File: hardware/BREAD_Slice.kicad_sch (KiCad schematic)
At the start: 15 parts, among them J1 Conn_01x10_Female, J2 I2C_01x04

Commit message: Initial commit
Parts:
- removed C1, C3, C4: 22uF, Capacitor_SMD:C_1206_3216Metric, symbol Device:C_Small
- removed C2: 100nF, Capacitor_SMD:C_1206_3216Metric, symbol Device:C_Small
- removed D1: WS2812B_5050, SparkFun-LED:WS2812-5050-4PIN, symbol SparkFun-LED:WS2812B_5050
- removed HS1: Heatsink_Pad, SparkFun-Fuse:Thermal Pad, symbol Mechanical:Heatsink_Pad
- removed J2: I2C_01x04, Connector_JST:JST_SH_SM04B-SRSS-TB_1x04-1MP_P1.00mm_Horizontal, symbol SparkFun-Connector:I2C_01x04
- removed L1: 4.7uH, Inductor_SMD:L_1210_3225Metric, symbol Device:L_Small
- removed U1: ~, Package_TO_SOT_SMD:TSOT-23-6, symbol SparkFun-DiscreteSemi:AP63205
- added C1, C2: 10uF_t, OCI_UPL_FOOTPRINTS:C_2312, symbol BREAD_Slice-rescue:10uF_t-OCI_UPL_2_Capacitors
- added J2, J3, J4, J5, J6: Screw_Terminal_01x03, TerminalBlock_TE-Connectivity:TerminalBlock_TE_282834-3_1x03_P2.54mm_Horizontal, symbol Connector:Screw_Terminal_01x03
- added J7: Conn_01x03_Male, Connector_PinSocket_2.54mm:PinSocket_1x03_P2.54mm_Vertical, symbol BREAD_Slice-rescue:Conn_01x03_Male-Connector
- added J8: Screw_Terminal_01x02, TerminalBlock_TE-Connectivity:TerminalBlock_TE_282834-2_1x02_P2.54mm_Horizontal, symbol Connector:Screw_Terminal_01x02
- added Logo1: Logo_Open_Hardware_Small, Symbol:OSHW-Symbol_6.7x6mm_SilkScreen, symbol Graphic:Logo_Open_Hardware_Small
- H1, H4: footprint MountingHole:MountingHole_5mm -> MountingHole:MountingHole_3.2mm_M3_DIN965_Pad
- H2: renamed from H3; footprint MountingHole:MountingHole_5mm -> MountingHole:MountingHole_3.2mm_M3_DIN965_Pad
- H3: renamed from H2; footprint MountingHole:MountingHole_5mm -> MountingHole:MountingHole_3.2mm_M3_DIN965_Pad
- J1: symbol Connector:Conn_01x10_Female -> BREAD_Slice-rescue:Conn_01x10_Female-Connector
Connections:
- net +12V: now also A1.30 (VIN), C1.1, J7.3 (Pin_3)
- net +5V: now also C2.1
- net GND: now also C1.2, C2.2, J2.3 (Pin_3), J3.3 (Pin_3), J4.3 (Pin_3), J5.3 (Pin_3), J6.3 (Pin_3), J8.2 (Pin_2)
- net PWM3: now reaches A1.12 (D9)
- net PWM3: now also J6.1 (Pin_1)
- net PWM4: now reaches A1.13 (D10)
- net PWM4: now also J3.1 (Pin_1)
- net PWM5: now reaches A1.14 (D11)
- net PWM5: now also J5.1 (Pin_1)
- net PWM2: now reaches A1.9 (D6)
- net PWM2: now also J4.1 (Pin_1)
- net LED renamed PWM1
- net PWM1: now also J2.1 (Pin_1)
- new net CSTM: J7.2 (Pin_2), J8.1 (Pin_1)
- new net PWR: J2.2 (Pin_2), J3.2 (Pin_2), J4.2 (Pin_2), J5.2 (Pin_2), J7.1 (Pin_1)
- no-connect marks 22 -> 16
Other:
- moved on the sheet: A1, H1, H2, H3, H4, J1

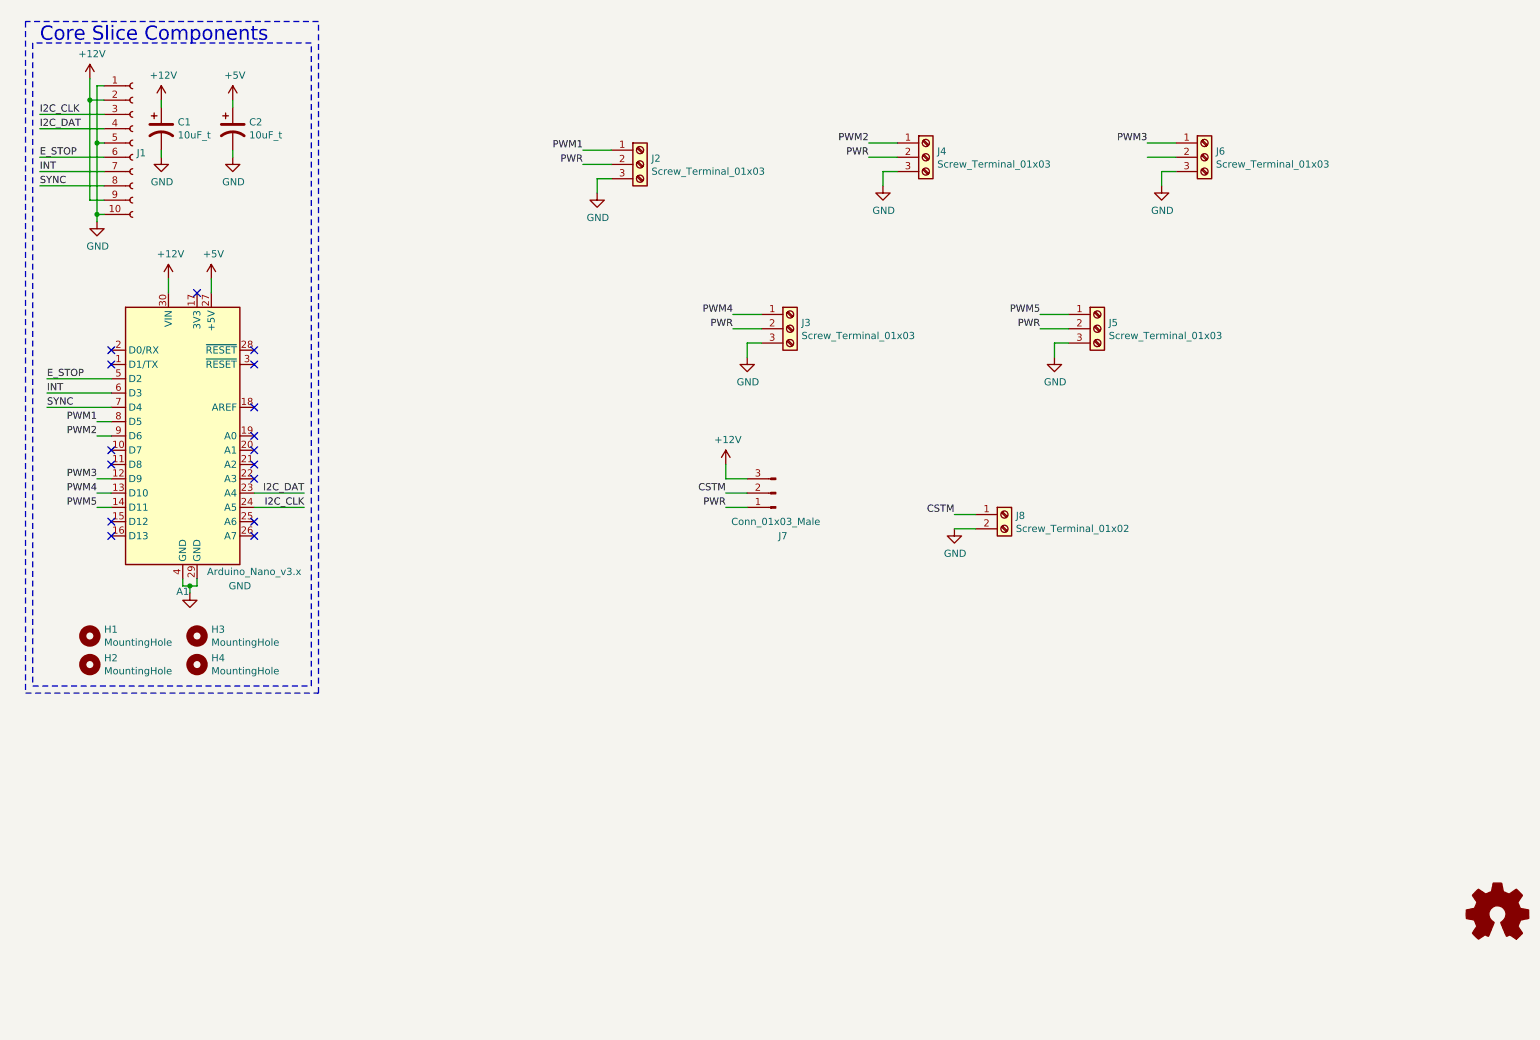
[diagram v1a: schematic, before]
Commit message: changed custom selection method to be correct and offer 5V, new BREAD core
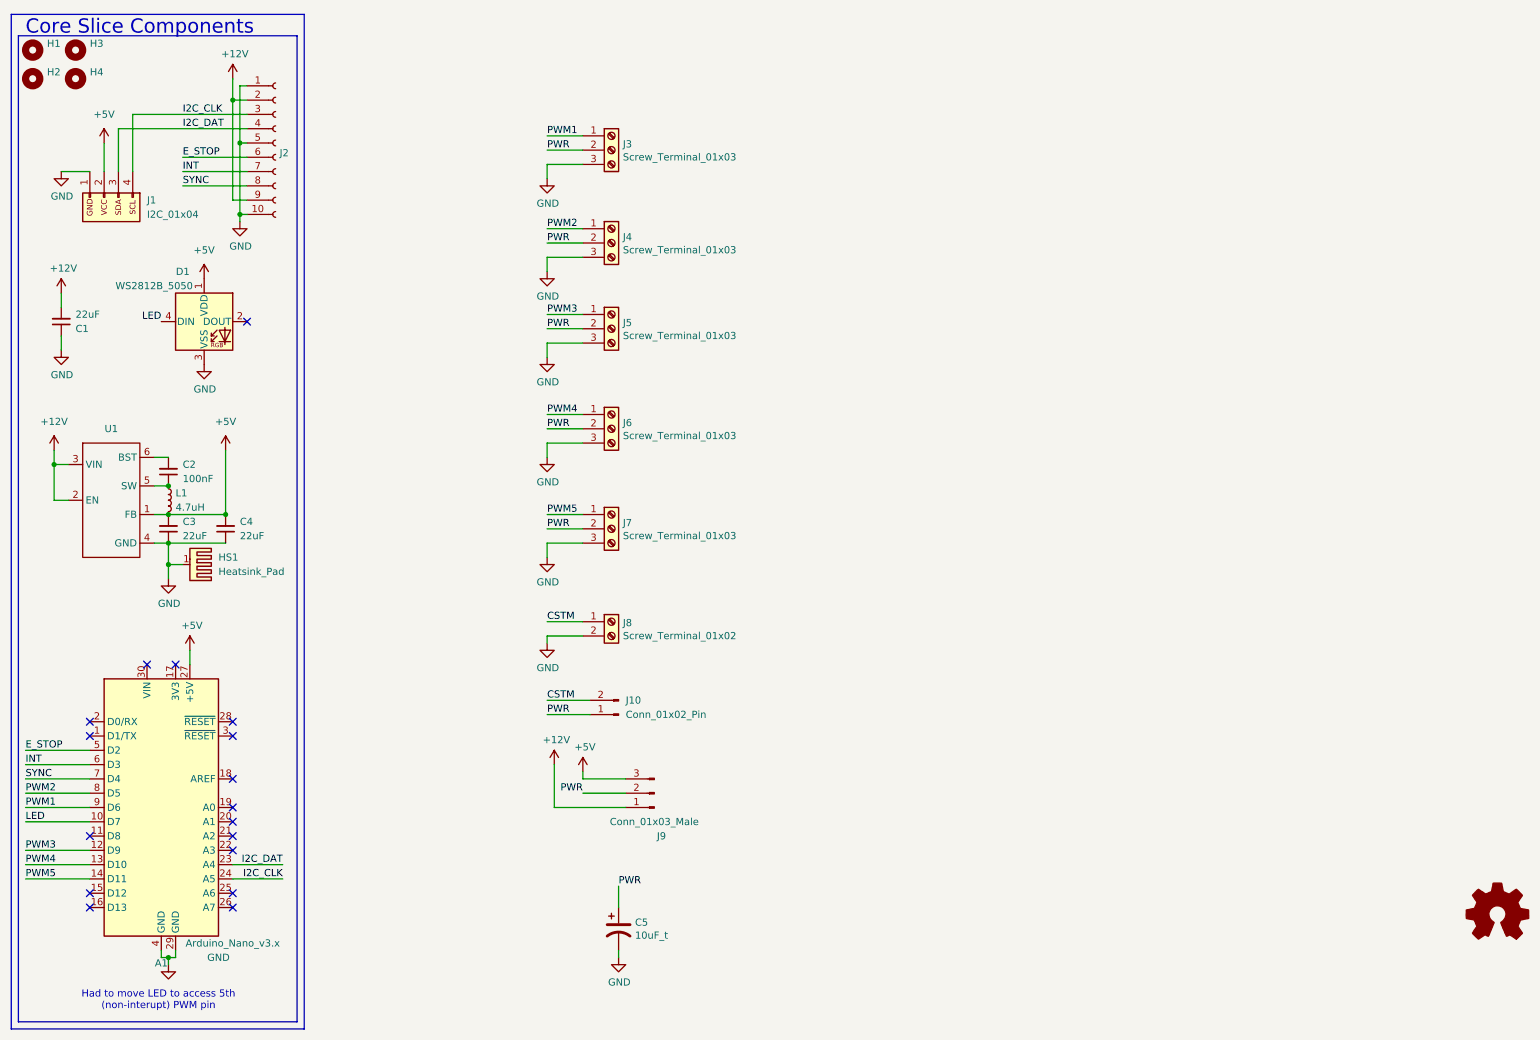
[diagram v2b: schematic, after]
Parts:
- removed C1, C2: 10uF_t, OCI_UPL_FOOTPRINTS:C_2312, symbol BREAD_Slice-rescue:10uF_t-OCI_UPL_2_Capacitors
- removed J2: Screw_Terminal_01x03, TerminalBlock_TE-Connectivity:TerminalBlock_TE_282834-3_1x03_P2.54mm_Horizontal, symbol Connector:Screw_Terminal_01x03
- removed J7: Conn_01x03_Male, Connector_PinSocket_2.54mm:PinSocket_1x03_P2.54mm_Vertical, symbol BREAD_Slice-rescue:Conn_01x03_Male-Connector
- removed Logo1: Logo_Open_Hardware_Small, Symbol:OSHW-Symbol_6.7x6mm_SilkScreen, symbol Graphic:Logo_Open_Hardware_Small
- added C1, C3, C4: 22uF, Capacitor_SMD:C_1206_3216Metric, symbol Device:C_Small
- added C2: 100nF, Capacitor_SMD:C_1206_3216Metric, symbol Device:C_Small
- added C5: 10uF_t, Capacitor_SMD:C_2220_5750Metric_Pad1.97x5.40mm_HandSolder, symbol BREAD_Slice-rescue:10uF_t-OCI_UPL_2_Capacitors
- added D1: WS2812B_5050, SparkFun-LED:WS2812-5050-4PIN, symbol SparkFun-LED:WS2812B_5050
- added HS1: Heatsink_Pad, KML-Custom:Thermal Pad, symbol Mechanical:Heatsink_Pad
- added J1: I2C_01x04, Connector_JST:JST_SH_SM04B-SRSS-TB_1x04-1MP_P1.00mm_Horizontal, symbol SparkFun-Connector:I2C_01x04
- added J10: Conn_01x02_Pin, Connector_PinSocket_2.54mm:PinSocket_1x02_P2.54mm_Vertical, symbol Connector:Conn_01x02_Pin
- added J7: Screw_Terminal_01x03, TerminalBlock_Phoenix:TerminalBlock_Phoenix_MPT-0,5-3-2.54_1x03_P2.54mm_Horizontal, symbol Connector:Screw_Terminal_01x03
- added J9: Conn_01x03_Male, Connector_PinSocket_2.54mm:PinSocket_1x03_P2.54mm_Vertical, symbol BREAD_Slice-rescue:Conn_01x03_Male-Connector
- added L1: 4.7uH, Inductor_SMD:L_1210_3225Metric, symbol Device:L_Small
- added U1: ~, Package_TO_SOT_SMD:TSOT-23-6, symbol SparkFun-DiscreteSemi:AP63205
- H1, H4: footprint MountingHole:MountingHole_3.2mm_M3_DIN965_Pad -> MountingHole:MountingHole_5mm
- H2: renamed from H3; footprint MountingHole:MountingHole_3.2mm_M3_DIN965_Pad -> MountingHole:MountingHole_5mm
- H3: renamed from H2; footprint MountingHole:MountingHole_3.2mm_M3_DIN965_Pad -> MountingHole:MountingHole_5mm
- J2: renamed from J1; symbol BREAD_Slice-rescue:Conn_01x10_Female-Connector -> Connector:Conn_01x10_Female
- J3, J4, J5, J6: footprint TerminalBlock_TE-Connectivity:TerminalBlock_TE_282834-3_1x03_P2.54mm_Horizontal -> TerminalBlock_Phoenix:TerminalBlock_Phoenix_MPT-0,5-3-2.54_1x03_P2.54mm_Horizontal
- J8: footprint TerminalBlock_TE-Connectivity:TerminalBlock_TE_282834-2_1x02_P2.54mm_Horizontal -> TerminalBlock_Phoenix:TerminalBlock_Phoenix_MPT-0,5-2-2.54_1x02_P2.54mm_Horizontal
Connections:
- net +12V: now also C1.2, J9.1 (Pin_1), U1.2 (EN), U1.3 (VIN); no longer A1.30 (VIN)
- net +5V: now also C3.2, C4.2, D1.1 (VDD), J1.2 (Pin_2), J9.3 (Pin_3), L1.2, U1.1 (FB)
- net CSTM: now also J10.2 (Pin_2)
- net GND: now also C1.1, C3.1, C4.1, C5.2, D1.3 (VSS), HS1.1, J1.1 (Pin_1), J7.3 (Pin_3), U1.4 (GND)
- net I2C_CLK: now also J1.4 (Pin_4)
- net I2C_DAT: now also J1.3 (Pin_3)
- net PWM1: now also A1.9 (D6), J3.1 (Pin_1); no longer A1.8 (D5)
- net PWM2: now also A1.8 (D5); no longer A1.9 (D6)
- net PWM3: now also J5.1 (Pin_1); no longer J6.1 (Pin_1)
- net PWM4: now also J6.1 (Pin_1); no longer J3.1 (Pin_1)
- net PWM5: now also J7.1 (Pin_1); no longer J5.1 (Pin_1)
- net PWR: now also J6.2 (Pin_2), C5.1, J10.1 (Pin_1), J7.2 (Pin_2), J9.2 (Pin_2)
- net LED: now reaches A1.10 (D7)
- net LED: now also D1.4 (DIN)
- new net: C2.1, L1.1, U1.5 (SW)
- new net: C2.2, U1.6 (BST)
- no-connect marks 16 -> 17
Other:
- note added: "Had to move LED to access 5th (non-interupt) PWM pin"
- moved on the sheet: A1, H1, H2, H3, H4, J2
